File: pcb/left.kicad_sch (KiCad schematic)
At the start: 119 parts, among them J101 OLED 0.96in I2C, Q101 AO3401A, Q102 AO3401A, Q103 AO3400A, SW101 =, SW102 1, SW103 2, SW104 3, SW105 4, SW106 5, SW108 Tab, SW109 Q, SW110 W, SW111 E, SW112 R, SW113 T, SW114 Esc, SW115 A, SW116 S, SW117 D, SW118 F, SW119 G, SW120 Alt, SW121 Shift, SW122 Z, SW123 X, SW124 C, SW125 V, SW126 B, SW127 Ctrl, SW128 `, SW129 Caps, SW130 Left, SW131 Right, SW132 Super, SW133 Bksp, SW134 Del, SW190 MSK12C02 power, SW191 Reset, U101 nRF52840 Pro Micro

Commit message: feat(layout): refine thumb cluster and OLED placement
Use 1.25u lower thumb keys, keep the upper pair at 1u, move the encoders and OLEDs, and align the board outline with the thumb row. Regenerate the routed PCB, case, plate, print sheets, fabrication files, BOM, and documentation.
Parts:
- SW133, SW134: footprint keygen:SW_MX_HS_CPG151101S11_1.5u -> keygen:SW_MX_HS_CPG151101S11_1.25u
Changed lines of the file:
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@@
     (property "Reference" "SW133" (at 233.68 156.21 0) (effects (font (size 1.27 1.27))))
     (property "Value" "Bksp" (at 233.68 168.91 0) (effects (font (size 1.27 1.27))))
-    (property "Footprint" "keygen:SW_MX_HS_CPG151101S11_1.5u"
+    (property "Footprint" "keygen:SW_MX_HS_CPG151101S11_1.25u"
       (at 233.68 162.56 0)
       (effects (font (size 1.27 1.27)) (hide yes))
@@
     (property "Reference" "SW134" (at 274.32 156.21 0) (effects (font (size 1.27 1.27))))
     (property "Value" "Del" (at 274.32 168.91 0) (effects (font (size 1.27 1.27))))
-    (property "Footprint" "keygen:SW_MX_HS_CPG151101S11_1.5u"
+    (property "Footprint" "keygen:SW_MX_HS_CPG151101S11_1.25u"
       (at 274.32 162.56 0)
       (effects (font (size 1.27 1.27)) (hide yes))

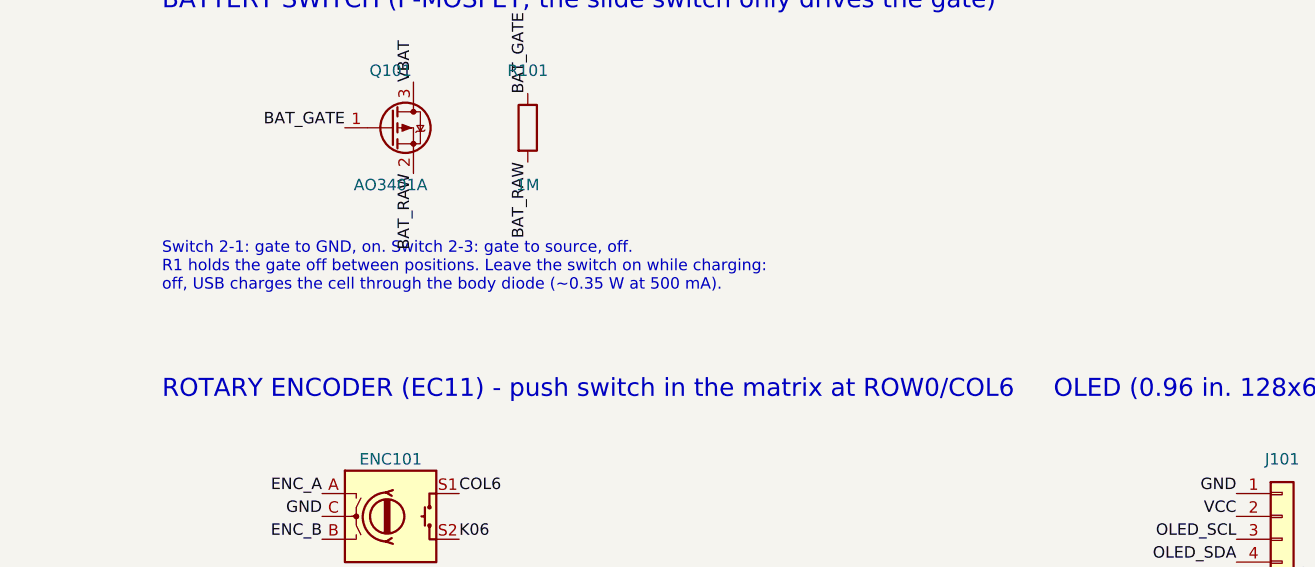
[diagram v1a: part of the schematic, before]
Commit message: chore(hardware): audit power, lighting, and assembly
Verify switch and LED geometry, net connectivity, firmware lighting behavior, and current limits. Record prototype checks and update build guidance and generated assets.
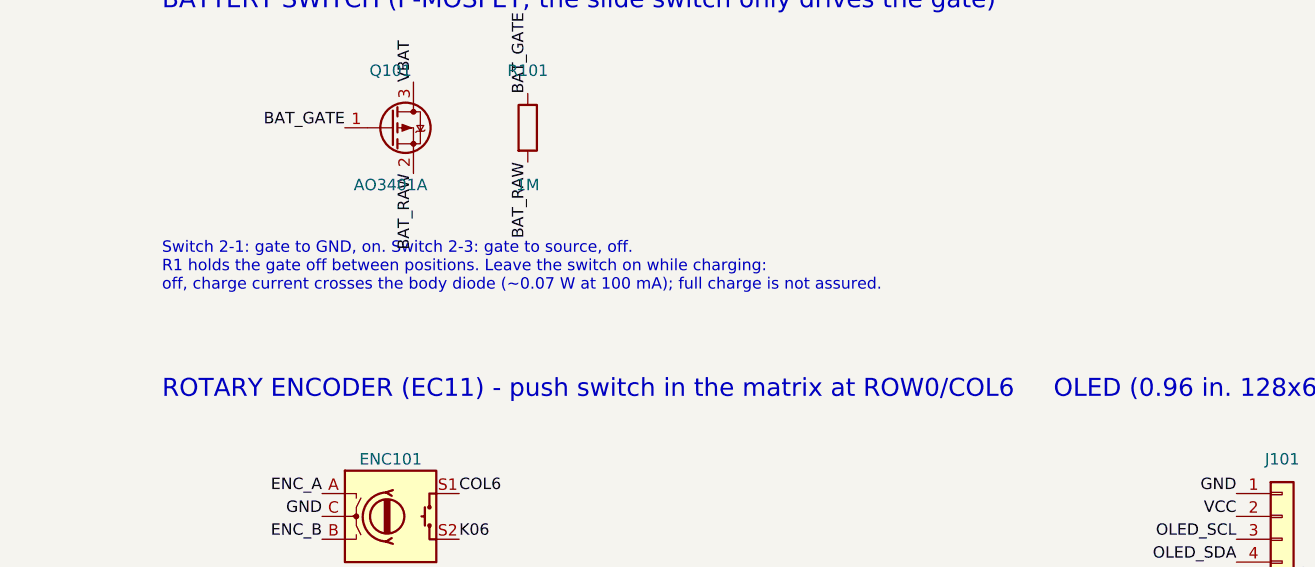
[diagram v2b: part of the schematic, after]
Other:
- note added: "Switch 2-1: gate to GND, on. Switch 2-3: gate to source, off. R1 holds the gate off between positions. Leave the switch on while charging: off, charge current crosses the body diode (~0.07 W at 100 mA); full charge is not assured."
- note removed: "Switch 2-1: gate to GND, on. Switch 2-3: gate to source, off. R1 holds the gate off between positions. Leave the switch on while charging: off, USB charges the cell through the body diode (~0.35 W at 500 mA)."
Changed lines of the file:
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@@
     (effects (font (size 1.27 1.27)) (justify right bottom))
   )
-  (text "Switch 2-1: gate to GND, on. Switch 2-3: gate to source, off.\nR1 holds the gate off between positions. Leave the switch on while charging:\noff, USB charges the cell through the body diode (~0.35 W at 500 mA)."
+  (text "Switch 2-1: gate to GND, on. Switch 2-3: gate to source, off.\nR1 holds the gate off between positions. Leave the switch on while charging:\noff, charge current crosses the body diode (~0.07 W at 100 mA); full charge is not assured."
     (exclude_from_sim no)
     (at 335.28 198.12 0)
